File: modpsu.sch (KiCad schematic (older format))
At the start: 28 parts, among them J1 OUT+, J2 OUT-, J4 IN, J5 IN, J6 OUT, Q10 AO4805, Q9 12A

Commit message: First working version
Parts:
- removed MP2: SCREW, mech:SCREW-4-SUPPORTED, symbol SCREW
- added R60, R61: 1k2, IPC7351-Nominal:RESC6432X70, symbol R-2512
- R1: value 2k -> 348; BOM RES SMD 2k 1% [0603] -> RES SMD 348 1% [0603]
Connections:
- net labels added: +3.3, +3.6, GND, OUT+, OUT-, PWR, V-
- net labels removed: PWRGND
- wire segments 99 -> 108
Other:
- note added: "24V"
- note added: "LOOP INTERFACE\n\nThe mainboard and all modules must be joined in a loop,\noutput of one connected to the input of the next. The sequence\nwill determine the logical ordering of the modules as seen\nby the user interface."
- note added: "MOD12003"
- moved on the sheet: C12, C13, C22, C23, D4, F1, F2, F3, J1, J2, J4, J5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

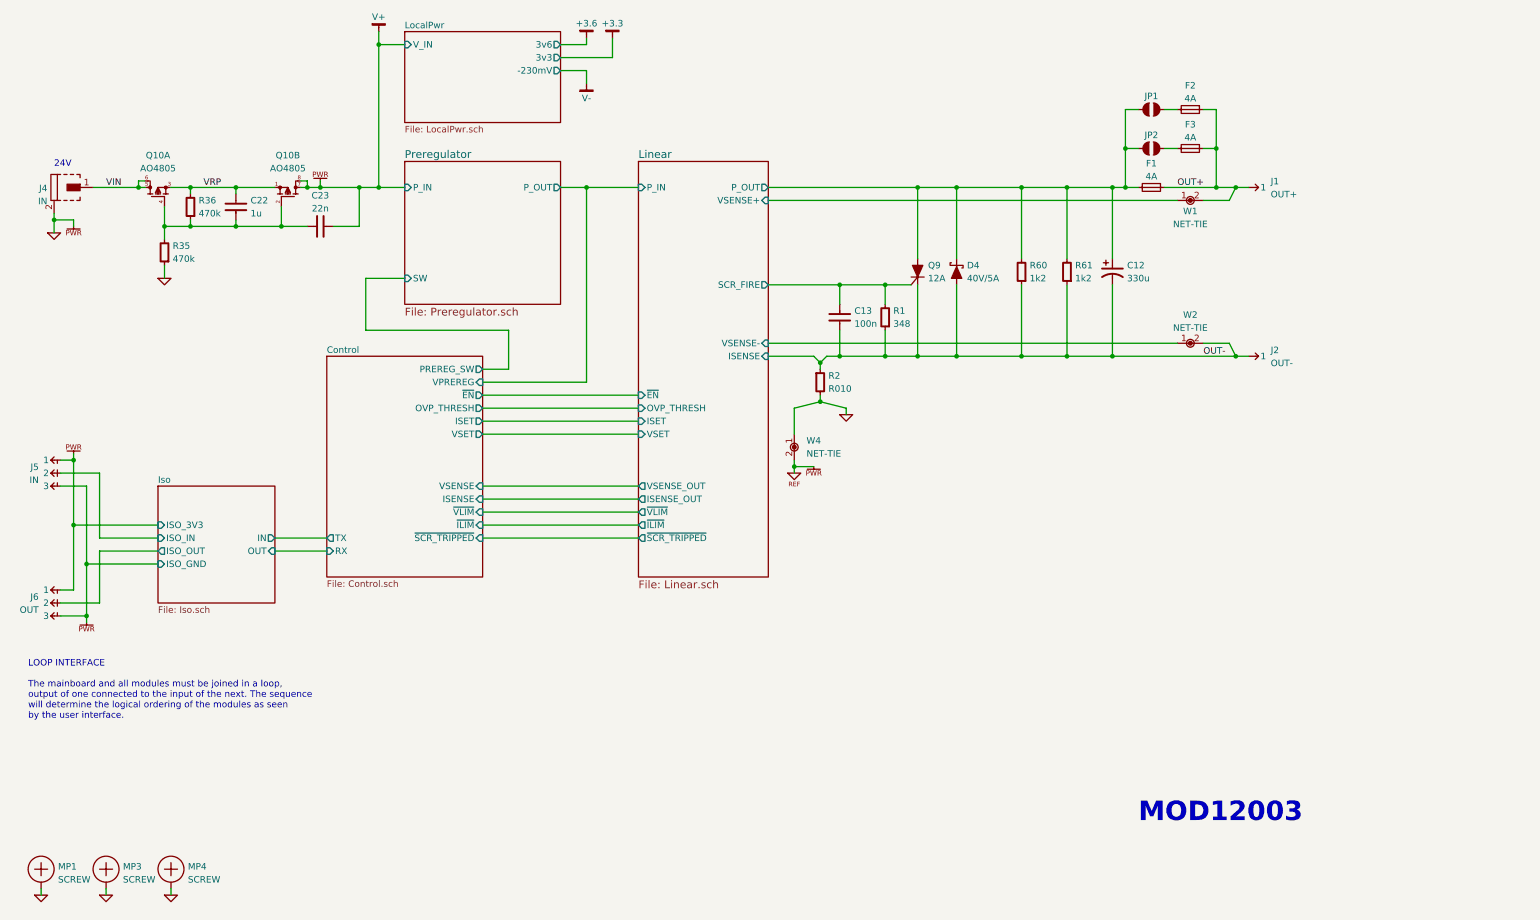
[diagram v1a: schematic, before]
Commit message: Reannotate component references
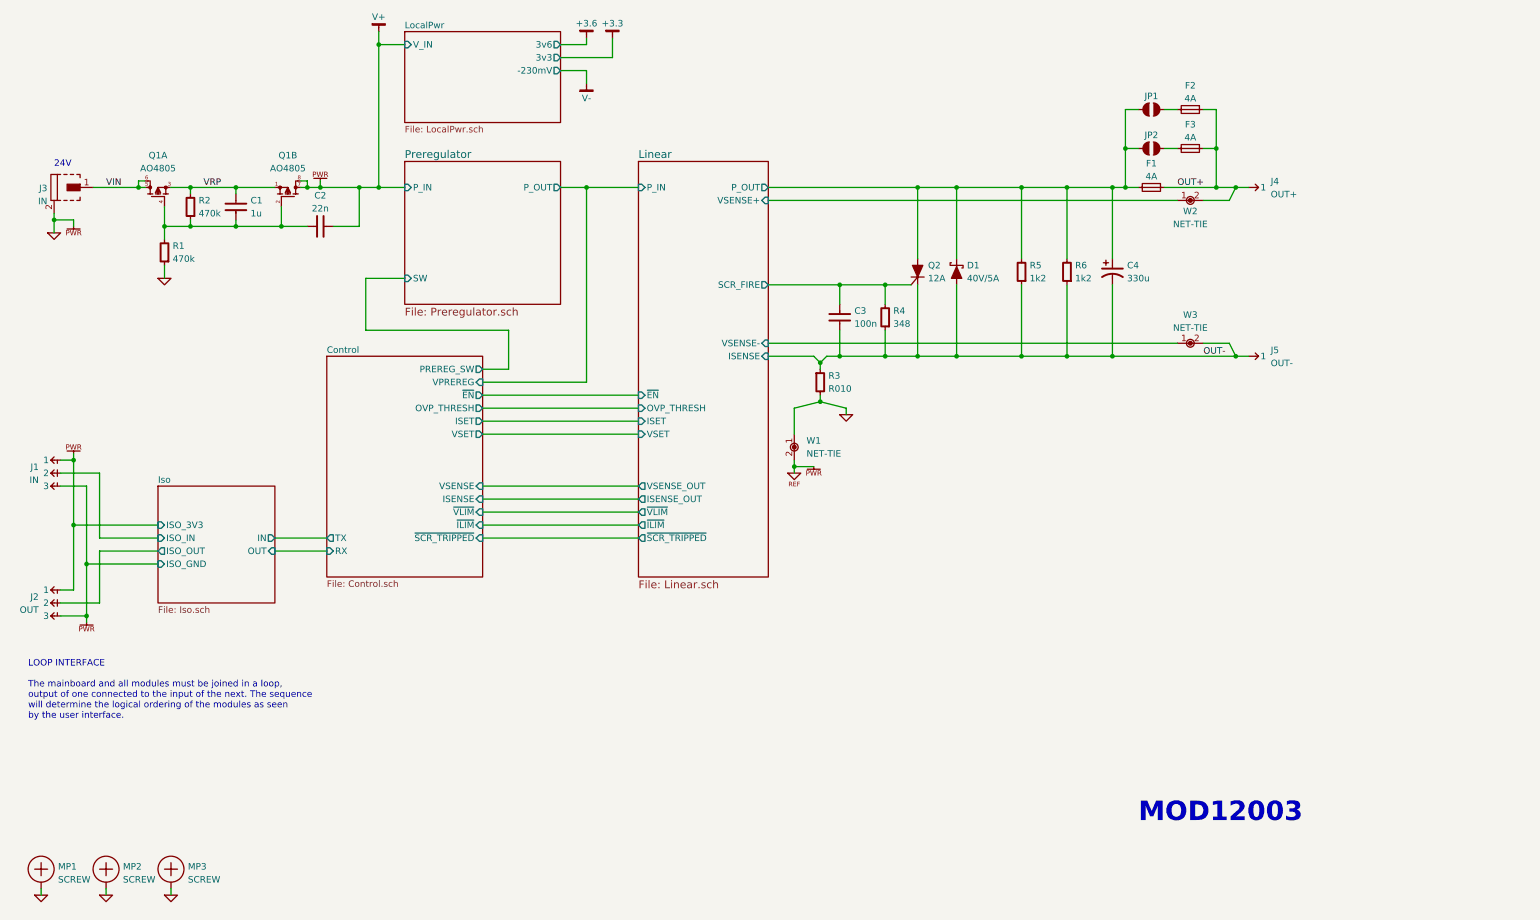
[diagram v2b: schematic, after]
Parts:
- renumbered C22 to C1, C23 to C2, C13 to C3, C12 to C4, D4 to D1, J5 to J1, J6 to J2, J4 to J3, J1 to J4, J2 to J5, MP3 to MP2, MP4 to MP3, Q10 to Q1, Q9 to Q2, R35 to R1, R36 to R2, R2 to R3, R1 to R4, R60 to R5, R61 to R6, W4 to W1, W1 to W2, W2 to W3

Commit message: Piles and piles of work
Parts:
- removed J1: IN, conn-100mil:CONN-100MIL-M-1x3-SHROUD, symbol CONN-100MIL-M-1x3-SHROUD
- removed J2: OUT, conn-100mil:CONN-100MIL-M-1x3-SHROUD, symbol CONN-100MIL-M-1x3-SHROUD
- added C58: 1k/1kV, IPC7351-Nominal:CAPC3216X70, symbol C-1206
- added J1: IN, conn-100mil:CONN-100MIL-M-1x4-SHROUD, symbol CONN-100MIL-M-1x4-SHROUD
- added J2: OUT, conn-100mil:CONN-100MIL-M-1x4-SHROUD, symbol CONN-100MIL-M-1x4-SHROUD
- added J8: DEVEL, conn-100mil:CONN-100MIL-M-1x3, symbol CONN-100MIL-M-1x3
- added JP3: JUMPER, conn-100mil:CONN-100MIL-M-1x2, symbol JUMPER
- added R52, R53: 470k, IPC7351-Nominal:RESC1608X50, symbol R-0603
- added SYM1: OSHW-SCHEM-PCB6mm, mech:OSHW-6mm, symbol OSHW-SCHEM-PCB6mm
- F1, F2, F3: BOM DIST DIGIKEY 507-1193-2-ND -> DIST DIGIKEY 507-1193-1-ND
- MP2, MP3: Value2 (none) -> NYLON
- R5, R6: value 1k2 -> 1k; BOM RES SMD 1k2 5% [2512] -> RES SMD 1k [2512]
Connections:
- net Control/RX: now also J8.2, JP3.2
- net Control/TX: now also J8.3
- net GND: now also C58.2, J8.1, R53.1; no longer MP1.1, MP2.1, MP3.1
- net Iso/ISO_GND: now also J1.1, J1.3, J2.1, J2.3
- net Iso/ISO_IN: now also J1.2
- net Iso/ISO_OUT: now also J2.2
- new net: R52.1, R53.2
- new net Iso/FROM_ISO_IN: JP3.1
- new net Iso/ISO_5V: J1.4, J2.4
- new net PAD_MP1: C58.1, MP1.1, R52.2
- new net PAD_MP2: MP2.1
- new net PAD_MP3: MP3.1
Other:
- note added: "90mm"
- note added: "@Q10"
- note added: "@Q10 and @U6 mount to heat sink,\nnot PCB, through a thin insulator.\neg. Laird A15037-003 (926-1489-ND)"
- note added: "@R5"
- note added: "@R6"
- note added: "@U6"
- note added: "METAL\nSCREW"
- note added: "MOUNTING/HEAT SINKING:"
- note added: "Mating connector: A30980-ND"
- note added: "SCREW"
- note added: "THERMAL ELASTOMER"
- note added: "Thermal elastomer pads can be cut from one of:\nt-Global H48-6-21-15-13-1A (1168-1700-ND)\nt-Global H48-6-25-25-9 (1168-1703-ND)\nor similar compressible materials.\n\nPlace an insulating plastic sheet between the PCB\nand the heat sink, with minimal cutouts for\npassthrough.\n\nTop two screws must be non-conductive."
- moved on the sheet: C1, C2, D1, MP1, MP2, Q2, R1, R2, R5, R6
